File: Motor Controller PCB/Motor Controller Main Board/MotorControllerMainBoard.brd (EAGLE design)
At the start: 100 x 100 mm, 86 parts, among them T1 TEENSY_3.1_ALL_PINS

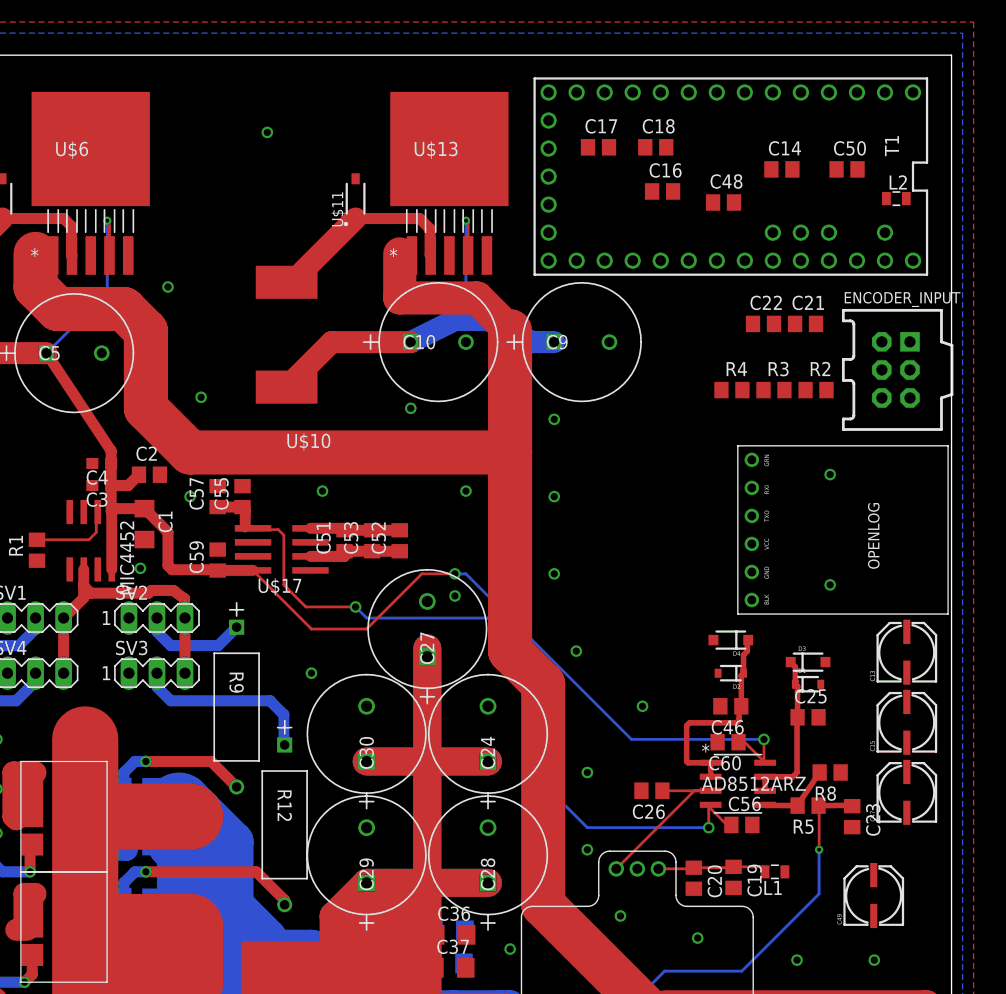
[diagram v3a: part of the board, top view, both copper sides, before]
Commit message: Moved teensy over
-makes wiring easier
-board is near completion
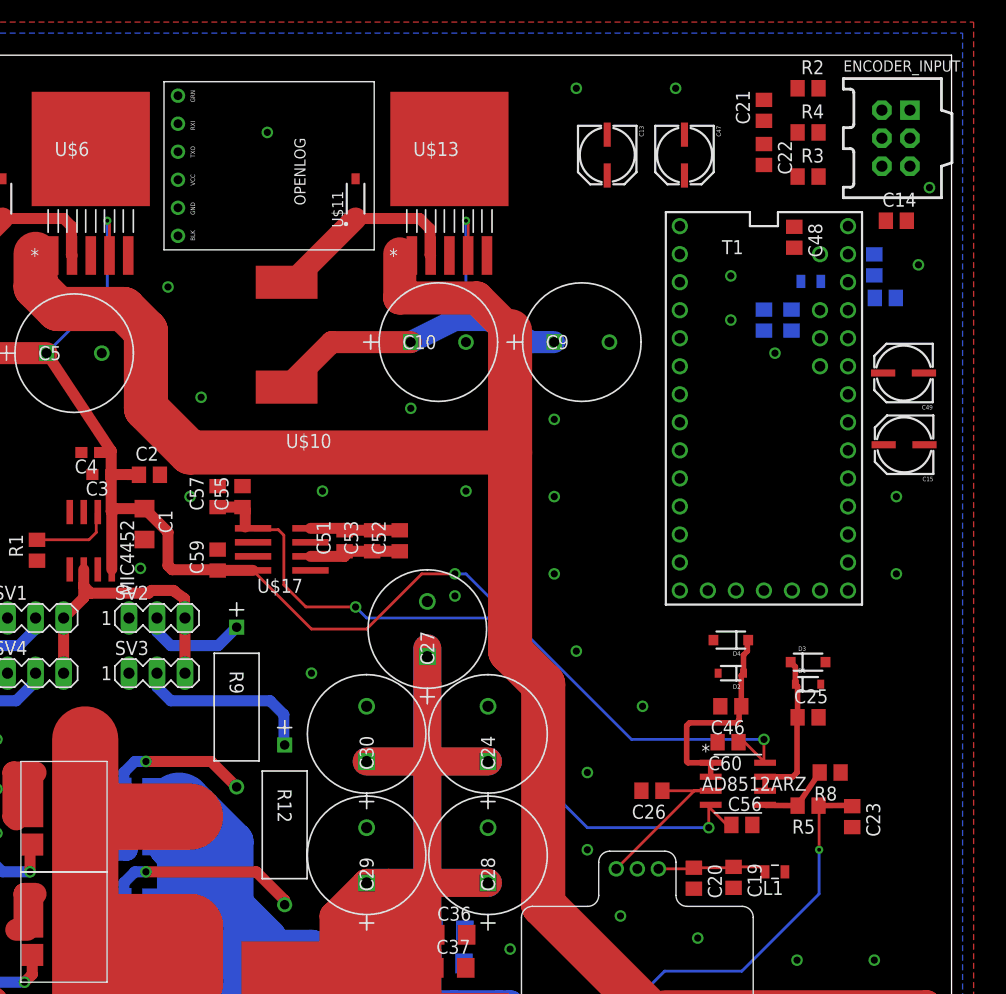
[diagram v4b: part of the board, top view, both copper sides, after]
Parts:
- moved O1 61.6 mm to (38.2, 90.0)
- moved C47 61.1 mm to (76.0, 91.0), turned to 270 degrees
- moved C13 52.5 mm to (69.0, 91.0), turned to 270 degrees
- moved C49 47.3 mm to (95.7, 71.0), turned to 180 degrees
- moved R2 27.4 mm to (87.0, 97.0)
- moved C15 25.0 mm to (95.8, 64.5), turned to 180 degrees
- moved R4 24.3 mm to (87.0, 93.0)
- moved C16 22.4 mm to (94.0, 78.0), flipped to the bottom, turned to 180 degrees
- moved C17 21.7 mm to (83.0, 76.0), flipped to the bottom, turned to 270 degrees
- moved T1 21.2 mm to (83.0, 68.0), turned to 0 degrees
- moved ENCODER_INPUT 21.0 mm to (95.0, 92.5)
- moved C18 19.9 mm to (85.5, 76.0), flipped to the bottom, turned to 270 degrees
- moved C21 19.7 mm to (83.0, 95.0), turned to 90 degrees
- moved R3 19.6 mm to (87.0, 89.0)
- moved C22 15.4 mm to (83.0, 91.0), turned to 270 degrees
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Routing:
- net 12V_POWER_REGULATED: track 141.1 -> 140.6 mm
- net GND: vias 36 -> 43

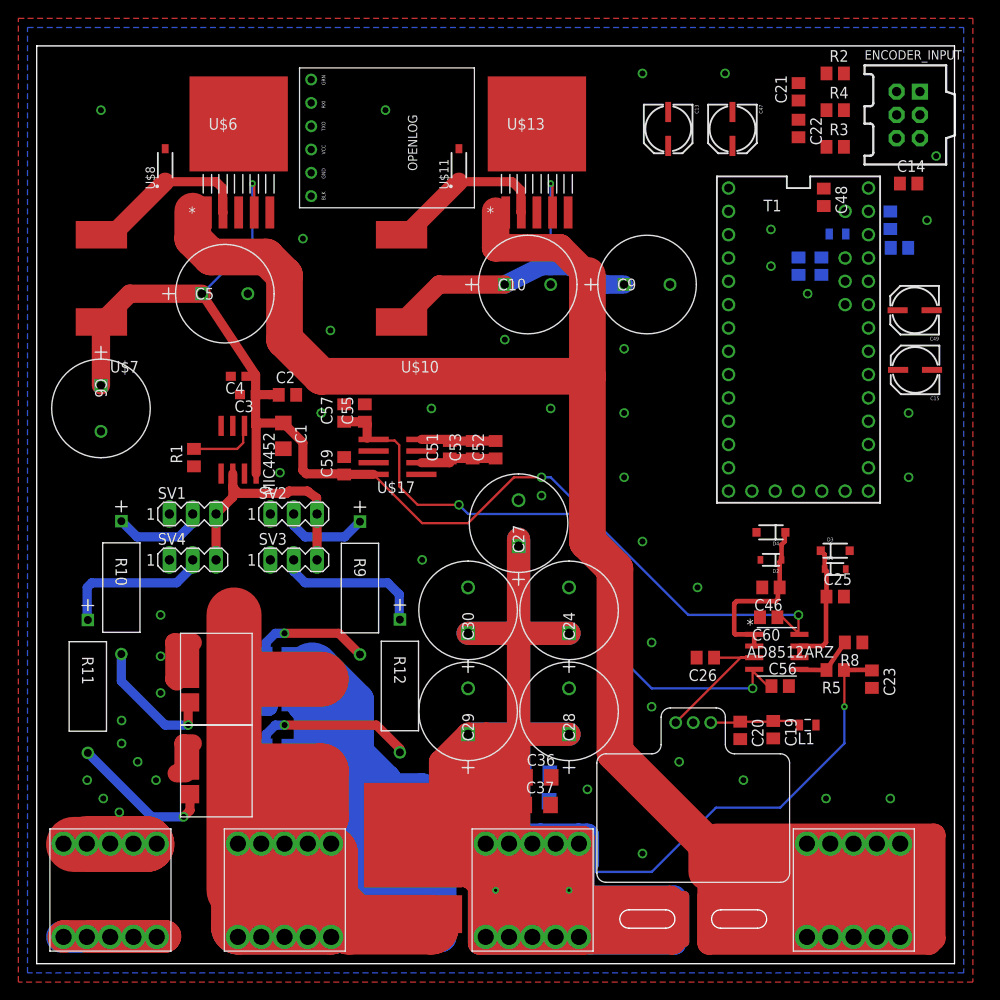
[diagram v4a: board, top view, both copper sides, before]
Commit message: Added digital connections
added digital connects, saving before routing them.
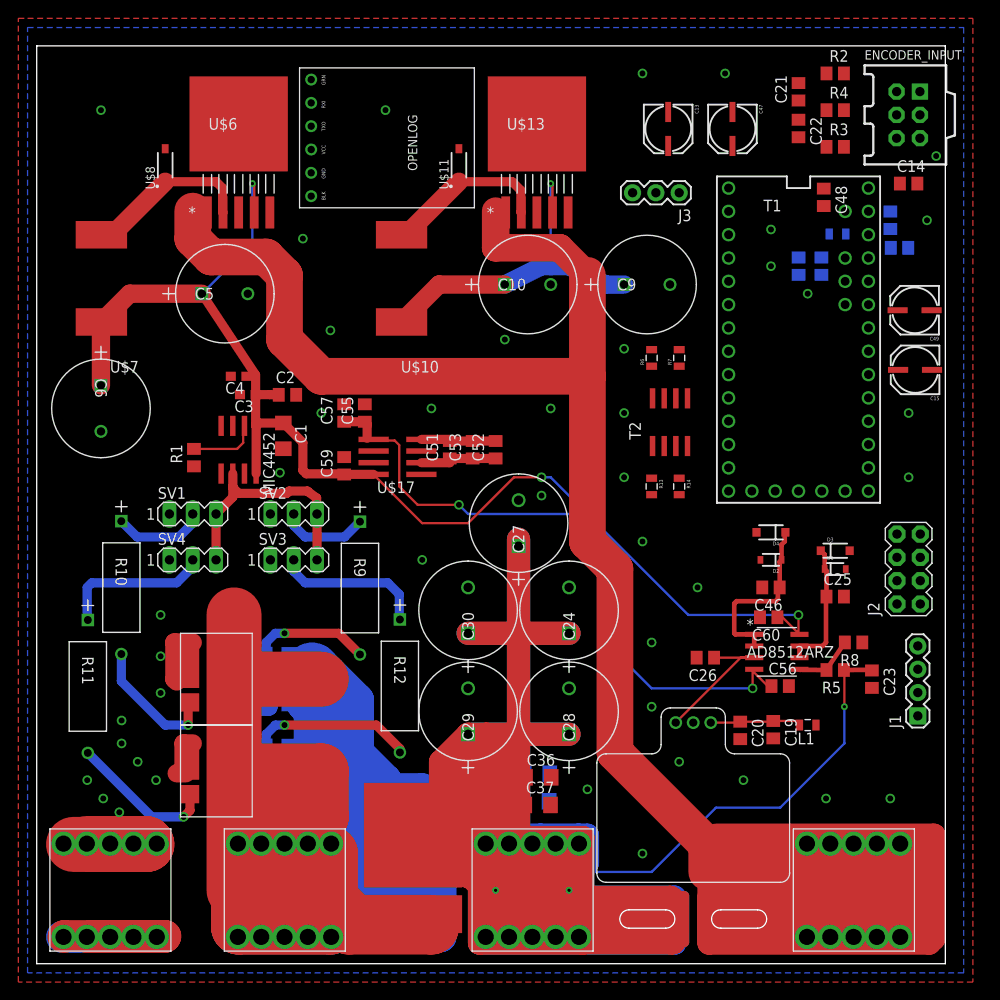
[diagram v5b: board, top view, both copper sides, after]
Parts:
- added J1: (no value), SparkFun-Connectors:1X04
- added J2: (no value), SparkFun-Connectors:2X4
- added J3: (no value), SparkFun-Connectors:1X03
- added R13, R14, R6, R7: 4.7k, SparkFun-Passives:0805
- added T2: (no value), zetex:SO8
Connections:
- new net BUTTON1: J2.5
- new net BUTTON2: J2.7
- new net HALL: J3.3, T1.10
- new net N$19: J1.3, R7.1, T2.5, T2.6
- new net N$20: J1.4, R6.1, T2.7, T2.8
- new net RX3: J2.8, T1.7
- new net SCL0: R14.1, T1.19/A5, T2.3
- new net SDA0: R13.1, T1.18/A4, T2.1
- new net TX3: J2.6, T1.8
- net 12V_POWER_REGULATED: now also J2.3
- net 3.3V_POWER_REGULATED: now also R13.2, R14.2, T2.2, T2.4
- net 5V_POWER_REGULATED: now also J1.2, J2.4, J3.2, R6.2, R7.2
- net GND: now also J1.1, J2.1, J2.2, J3.1
- net SUPPLY_VOLTAGE: now also T1.22/A8; no longer T1.18/A4
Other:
- board size 100 x 100 mm -> 99 x 100 mm

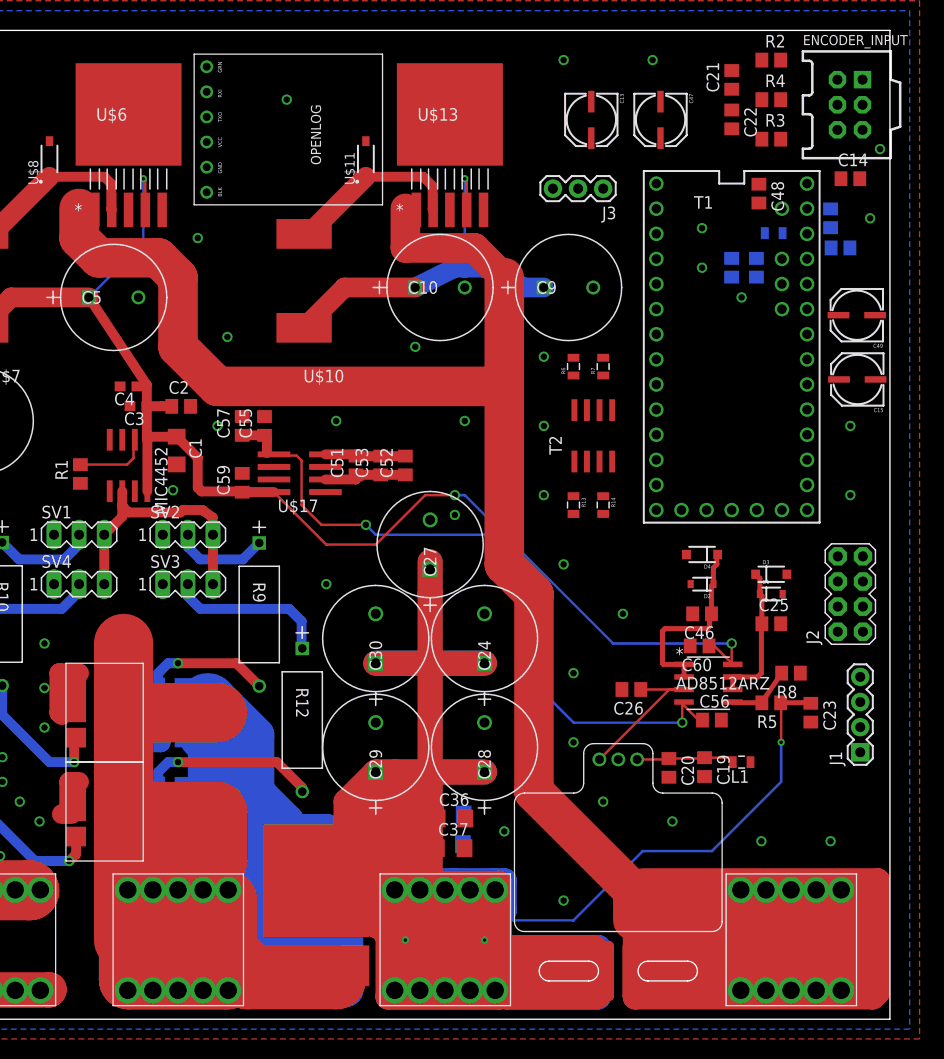
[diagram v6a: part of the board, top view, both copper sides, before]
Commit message: Used Autorouter
Used autorouter (I was tired and wanted to sleep since its 1:30am). It
looks fine, can fix a few things later.
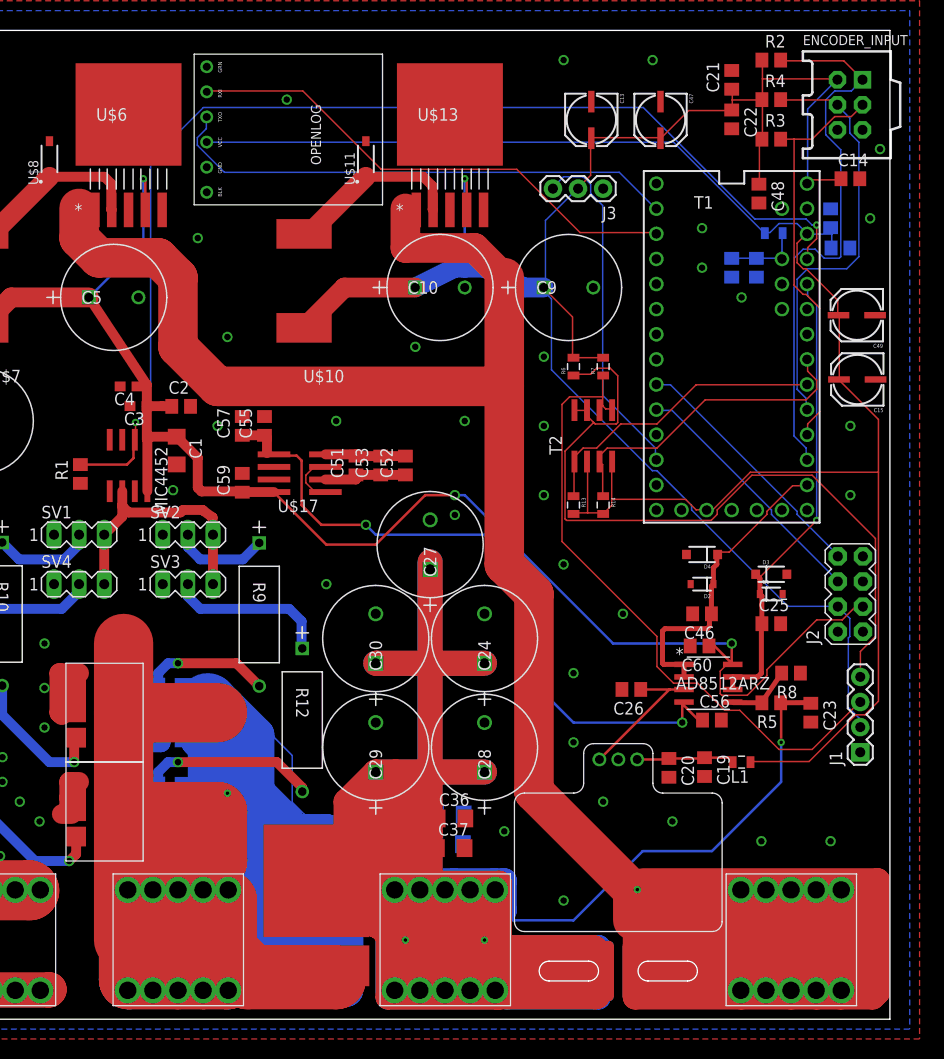
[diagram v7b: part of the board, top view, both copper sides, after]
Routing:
- net 3.3V_POWER_REGULATED: track 0.00 -> 180.6 mm
- net 5V_POWER_REGULATED: track 39.1 -> 185.0 mm
- net TEENSY_FET_DRIVER_SIGNAL: track 7.55 -> 114.8 mm, vias 0 -> 2
- net N$20: track 0.00 -> 77.1 mm
- net N$19: track 0.00 -> 65.8 mm
- net ENCODER_A: track 0.00 -> 56.6 mm
- net RX1: track 0.00 -> 52.3 mm
- net TX1: track 0.00 -> 51.5 mm
- net MOTOR_OUTPUT_(--): track 358.6 -> 405.6 mm, vias 0 -> 1
- net INDEX: track 0.00 -> 43.0 mm
- net ENCODER_B: track 0.00 -> 41.4 mm
- net HALL: track 0.00 -> 35.3 mm
- net SUPPLY_VOLTAGE: track 14.6 -> 47.1 mm, vias 0 -> 1
- net SCL0: track 0.00 -> 32.4 mm
- net SDA0: track 0.00 -> 30.6 mm
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
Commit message: Tweaks to traces
-just did some spot patching.
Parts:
- moved C15 0.50 mm to (95.2, 64.5)
- moved C49 0.50 mm to (95.2, 71.0)
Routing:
- net GND: track 89.1 -> 184.5 mm, vias 43 -> 55
- net TX1: track 51.5 -> 70.5 mm, vias 0 -> 2
- net 3.3V_POWER_REGULATED: track 180.6 -> 182.3 mm
- net MOTOR_OUTPUT_(--): vias 1 -> 2
